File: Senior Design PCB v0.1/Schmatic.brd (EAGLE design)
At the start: 90.2 x 65.7 mm, 233 parts, among them IC1 TMC2208, IC2 TMC2208, IC3 TMC2208, IC4 TMC2208, IC5 TMC2208, IC6 CP2104, Q1 mmbt2222, Q2 mmbt2222, Q3 MMBT4403, Q4 AOD417, Q5 MMBT4403, Q6 MMBT4403, Q7 DMG3415U, U1 PCA9685, U2 AP2112-3.3, U3 HTU21DF, U4 HX711, U5 HX711, U6 HX711, X2 ESP32_WROOM32_SKINNY

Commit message: done all routing
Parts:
- removed C15, C22, C29: 0.1uF, SparkFun-Capacitors:0603-CAP
- removed C3: 560uF, SparkFun-Capacitors:PANASONIC_G
- removed D3: RED, microbuilder:CHIPLED_0805_NOOUTLINE
- removed R10: 1K, microbuilder:0603-NO@1
- moved U$4 19.2 mm to (-2.51, 4.82)
- moved U$48 18.4 mm to (92.2, 4.97)
- moved C68 13.5 mm to (6.86, 32.0), turned to 0 degrees
- moved R13 10.2 mm to (26.2, 48.0), turned to 270 degrees
- moved R34 8.92 mm to (55.1, 17.0)
- moved R52 8.03 mm to (26.7, 25.4), turned to 90 degrees
- moved R32 7.82 mm to (78.7, 23.6), turned to 0 degrees
- moved R31 6.68 mm to (79.8, 23.9), turned to 0 degrees
- moved SJ3 5.79 mm to (24.9, 42.2)
- moved C25 5.36 mm to (15.0, 54.9), turned to 270 degrees
- moved R1 4.77 mm to (61.7, 50.0), turned to 180 degrees
- moved R55 4.31 mm to (11.9, 10.9)
- moved R54 3.97 mm to (34.8, 22.9), turned to 270 degrees
- moved R28 3.75 mm to (78.0, 12.2), turned to 0 degrees
- moved C57 3.09 mm to (37.3, 17.3)
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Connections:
- net EN_3 renamed EN_LIQUID_1
- net EN_4 renamed EN_LIQUID_3
- net EN_5 renamed EN_LIQUID_2
- removed net DIR_3: IC3.19
- removed net DIR_4: IC4.19
- removed net DIR_5: IC5.19
- removed net EN_1: IC1.2, R33.2
- removed net EN_2: IC2.2, R40.2
- removed net MS1_1: IC1.9
- removed net MS1_2: IC2.9
- removed net MS1_3: IC3.9
- removed net MS1_4: IC4.9
- removed net MS1_5: IC5.9
- removed net MS2_1: IC1.10
- removed net MS2_2: IC2.10
- removed net MS2_3: IC3.10
- removed net MS2_4: IC4.10
- removed net MS2_5: IC5.10
- removed net N$5: D3.A, R10.2
- removed net STEP_3: IC3.16
- removed net STEP_4: IC4.16
- removed net STEP_5: IC5.16
- removed net VDD: C15.1, C22.1, C29.1
- new net DIR_LIQUID: IC3.19, IC4.19, IC5.19
- new net EN_XY: IC1.2, IC2.2, R33.2, R40.2
- new net MS1_LIQUID: IC3.9, IC4.9, IC5.9
- new net MS1_SOLID: IC1.9, IC2.9
- new net MS2_LIQUID: IC3.10, IC4.10, IC5.10
- new net MS2_SOLID: IC1.10, IC2.10
- new net STEP_LIQUID: IC3.16, IC4.16, IC5.16
- net 5V_SERVO: no longer C3.+
- net GND: no longer C15.2, C22.2, C29.2, C3.-, D3.C
- net ONBOARD_LED: no longer R10.1
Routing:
- net 5V_SERVO: track 4.20 -> 115.3 mm, vias 21 -> 53
- net SDA: track 5.41 -> 112.4 mm, vias 0 -> 4
- net SCL: track 5.88 -> 101.3 mm, vias 0 -> 3
- net VCC: track 9.40 -> 102.6 mm, vias 3 -> 36
- net 5V_REG: track 0.00 -> 89.7 mm, vias 18 -> 27
- net N$39: track 0.00 -> 65.3 mm
- net GND: track 321.4 -> 386.3 mm, vias 199 -> 193
- net N$40: track 0.00 -> 64.5 mm
- net N$38: track 0.00 -> 60.9 mm
- net MS2_LIQUID: track 0.00 -> 55.5 mm, vias 0 -> 4
- net N$50: track 0.00 -> 52.8 mm
- net RXD0: track 0.00 -> 52.0 mm, vias 0 -> 2
- net N$41: track 0.00 -> 51.9 mm, vias 0 -> 3
- net 12V_REG: track 23.6 -> 74.1 mm, vias 8 -> 19
- net MS1_LIQUID: track 0.00 -> 49.8 mm, vias 0 -> 3
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- added copper zone on layer 2, net 5V_SERVO
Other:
- board size 90.2 x 65.7 mm -> 101.3 x 66.8 mm

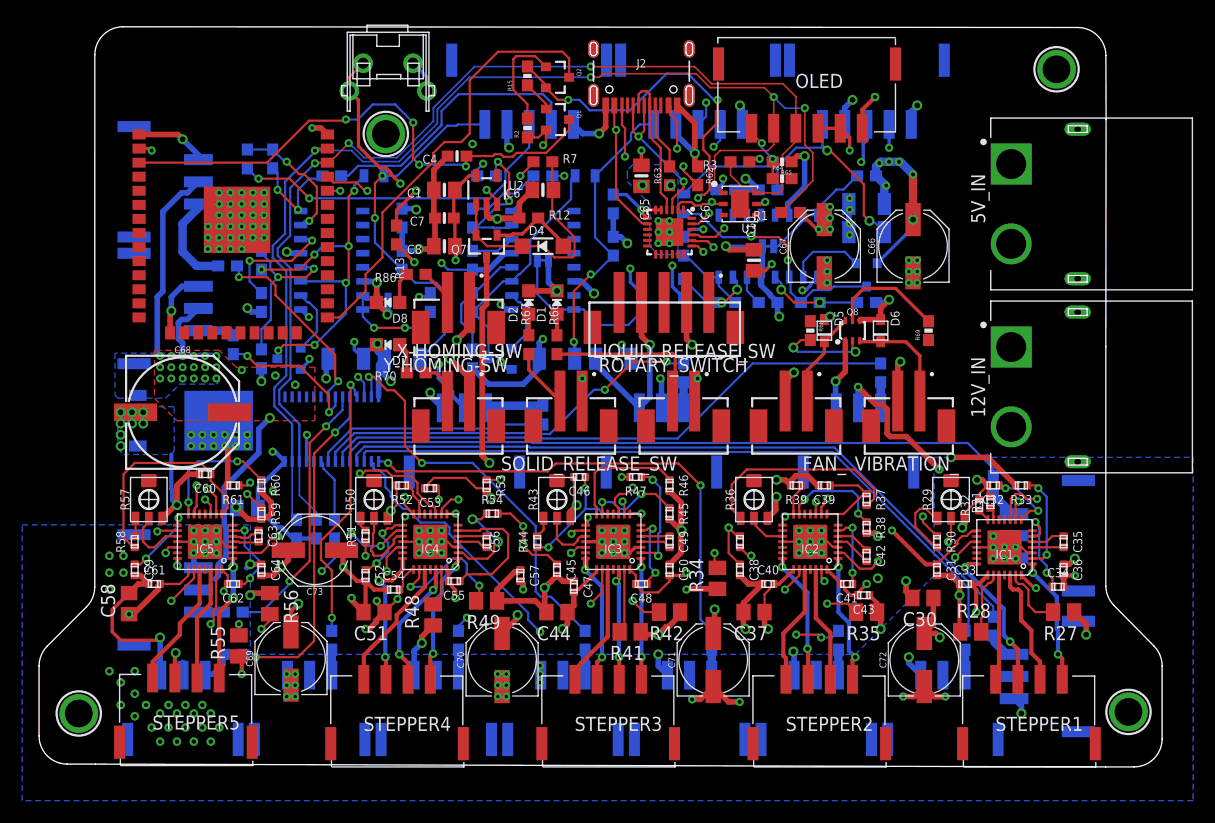
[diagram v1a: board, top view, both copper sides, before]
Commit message: update on i2c expander, fixed current pour
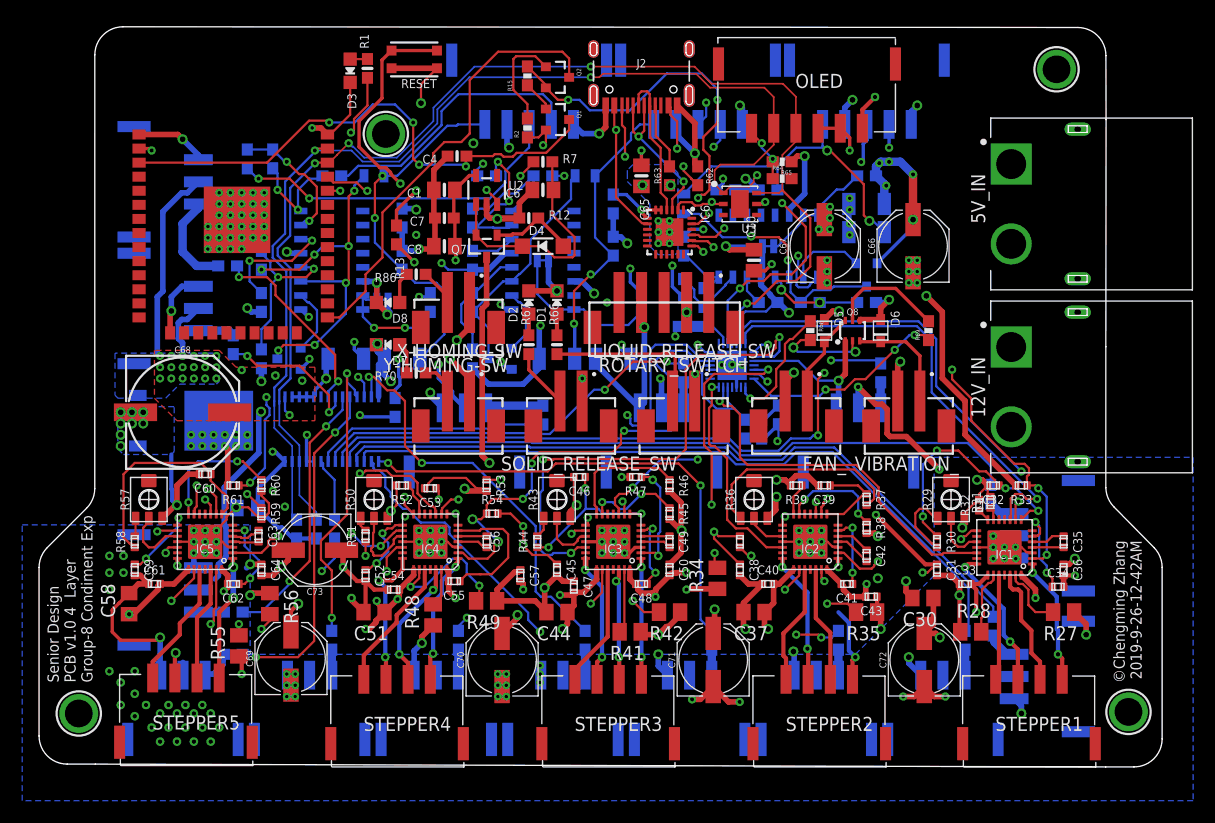
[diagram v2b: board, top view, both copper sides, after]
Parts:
- removed R3: 10k, SparkFun-Resistors:0603
- removed U$9: RIGHT_ANGLE_TACTILE_SWITCH, NewKevinMade:RIGHT_ANGLE_TACTILE_SWITCH
- added C15, C22, C3: 0.1uF, SparkFun-Capacitors:0603-CAP
- added D3: POWER, microbuilder:CHIPLED_0805_NOOUTLINE
- added R10: 10K, SparkFun-Resistors:0603-RES
- added R90: 10k, SparkFun-Resistors:0603
- added RESET: KMR2, microbuilder:BTN_KMR2_4.6X2.8
- added U7: SX1509, SparkFun-DigitalIC:QFN-28
- C11, C12, C13, C14, C18, C19, C20, C21, C25, C26, C27, C28: device SparkFun-Capacitors:0603-CAP -> SparkFun-Capacitors:0603-CAP@1
- R1: value 10k -> 1K; device SparkFun-Resistors:0603 -> microbuilder:0603-NO
- R11, R14, R17, R18, R19, R20, R22, R23, R24, R25, R5, R9: device SparkFun-Resistors:0603-RES -> SparkFun-Resistors:0603-RES@1
- R12, R66, R67, R7, R70, R86: device microbuilder:0603-NO@1 -> microbuilder:0603-NO
- SJ1, SJ2, SJ3: value (none) -> JUMPER-PAD-2-NC_BY_TRACE
- moved R1 40.3 mm to (23.5, 63.0), turned to 90 degrees
- moved C11 2.02 mm to (53.9, 42.4), turned to 90 degrees
- moved R71 0.83 mm to (79.8, 24.6)
- moved C43 0.69 mm to (69.0, 15.4)
- renumbered U$2 to WEIGHT3, U$5 to WEIGHT1, WEIGHT_SENSOR to WEIGHT2
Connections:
- removed net A0: U1.1
- removed net A1: U1.2
- removed net A2: U1.3
- removed net A3: U1.4
- removed net A4: U1.5
- removed net A5: U1.24
- new net !INT: U7.9
- new net !RESET: R10.1, U7.23
- new net 10: U7.15
- new net 11: U7.16
- new net 15: U7.22
- new net N$30: R90.1, U1.1
- new net N$5: D3.A, R1.2
- new net OSCIO: U7.11
- net DIR_1: now also U7.13
- net DIR_2: now also U7.14
- net DIR_LIQUID: now also U7.2
- net EN_LIQUID_1: now also U7.20
- net EN_LIQUID_2: now also U7.21
- net EN_LIQUID_3: now also U7.19
- net EN_XY: now also U7.1
- net FAN: now also U7.8
- net GND: now also C15.2, C22.2, C3.2, D3.C, RESET.A, RESET.A', U1.2, U1.24, U1.3, U1.4, U1.5, U7.10, U7.17, U7.26, U7.29, U7.3; no longer U$9.B_L, U$9.T_L
- net MS1_LIQUID: now also U7.5
- net MS1_SOLID: now also U7.27
- net MS2_LIQUID: now also U7.6
- net MS2_SOLID: now also U7.28
- net N$54: now also RESET.B, RESET.B'; no longer U$9.B_R, U$9.T_R
- net SCL: now also U7.25; no longer R3.2
- net SDA: now also U7.24; no longer R1.2
- net VCC: now also C15.1, C22.1, C3.1, R10.2, R90.2, U7.12, U7.18, U7.4; no longer R3.1
- net VIB: now also U7.7
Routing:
- net EN_LIQUID_2: track 12.0 -> 63.3 mm, vias 2 -> 4
- net DIR_LIQUID: track 45.0 -> 90.6 mm, vias 3 -> 5
- net GND: track 386.3 -> 427.5 mm, vias 193 -> 198
- net EN_XY: track 42.9 -> 83.3 mm, vias 4 -> 6
- net MS1_SOLID: track 22.3 -> 60.0 mm, vias 2 -> 3
- net MS2_SOLID: track 28.4 -> 63.7 mm
- net EN_LIQUID_3: track 9.44 -> 44.4 mm, vias 2 -> 5
- net DIR_1: track 0.00 -> 33.4 mm, vias 0 -> 1
- net MS1_LIQUID: track 49.8 -> 79.1 mm, vias 3 -> 6
- net VCC: track 102.6 -> 129.3 mm, vias 36 -> 37
- net EN_LIQUID_1: track 10.0 -> 32.2 mm, vias 2 -> 3
- net 5V_REG: track 89.7 -> 109.8 mm, vias 27 -> 29
- net DIR_2: track 0.00 -> 19.6 mm, vias 0 -> 1
- net VIB: track 0.00 -> 18.9 mm, vias 0 -> 3
- net MS2_LIQUID: track 55.5 -> 73.7 mm, vias 4 -> 6
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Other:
- outline, holes or cut-outs redrawn
- board text added: "Senior Design PCB v1.0 4 Layer Group-8 Condiment Exp"
- board text added: "©Chengming Zhang 2019-9-26-12-42AM"

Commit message: added contact board
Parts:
- removed SJ1, SJ2, SJ3: JUMPER-PAD-2-NC_BY_TRACE, SparkFun-Passives:PAD-JUMPER-2-NC_BY_TRACE_YES_SILK
- moved U$49 21.6 mm to (4.50, 63.1)
- moved R13 13.0 mm to (26.7, 61.0), turned to 0 degrees
- moved D3 12.1 mm to (9.85, 62.8), turned to 90 degrees
- moved R1 10.4 mm to (13.2, 62.9), turned to 180 degrees
- moved RESET 7.30 mm to (20.5, 63.2), turned to 0 degrees
- moved X2 6.48 mm to (5.08, 50.8), turned to 90 degrees
- moved R22 5.24 mm to (14.0, 49.8)
- moved R30 2.84 mm to (73.7, 22.9), turned to 0 degrees
- moved C25 1.80 mm to (13.7, 53.6)
- moved R40 1.72 mm to (57.2, 18.6)
- moved R82 1.44 mm to (11.1, 46.6)
- moved R71 1.27 mm to (79.8, 23.3)
- moved SERVO12 1.27 mm to (90.2, 25.4)
- moved C33 1.27 mm to (77.5, 15.2)
- moved C37 1.27 mm to (58.4, 12.7)
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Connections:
- removed net A13_I35: X2.7
- removed net A2_I34: X2.6
- removed net A5_IO4: X2.26
- removed net BUZZER: X2.10
- removed net CAP_OR_BAT: X2.14
- removed net CHARGE_OR_NOT: X2.16
- removed net IO15_A8: X2.23
- removed net IO21: X2.33
- removed net IO32_A7: X2.8
- removed net MISO: X2.31
- removed net MOSI: X2.30
- removed net N$10: R16.1, SJ2.2, U4.15, U4.16
- removed net N$18: R21.1, SJ1.2, U5.15, U5.16
- removed net N$25: R26.1, SJ3.2, U6.15, U6.16
- removed net ONBOARD_LED: X2.13
- removed net RX_CUS: X2.12
- removed net SCK: X2.29
- removed net SD_CS_MCU: X2.9
- removed net TX_CUS: X2.11
- net GND: now also R16.1, R21.1, R26.1, U4.15, U4.16, U5.15, U5.16, U6.15, U6.16; no longer SJ1.1, SJ2.1, SJ3.1
- net LRSW: now also X2.16
- net ROTA_A: now also X2.33
- net ROTA_C: now also X2.12
- net ROTA_E: now also X2.23
- net SRSW: now also X2.30
- net STEP_1: now also X2.26
- net STEP_2: now also X2.29
- net STEP_LIQUID: now also X2.31
- net WEIGHT_CLK_1: now also X2.9
- net WEIGHT_CLK_2: now also X2.11
- net WEIGHT_CLK_3: now also X2.14
- net WEIGHT_DATA_1: now also X2.8
- net WEIGHT_DATA_2: now also X2.10
- net WEIGHT_DATA_3: now also X2.13
- net X-HOMING: now also X2.6
- net Y-HOMING: now also X2.7
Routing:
- net STEP_1: track 0.00 -> 102.0 mm, vias 0 -> 9
- net STEP_2: track 0.00 -> 83.7 mm, vias 0 -> 5
- net WEIGHT_CLK_1: track 0.00 -> 77.2 mm, vias 0 -> 6
- net WEIGHT_DATA_1: track 0.00 -> 70.5 mm, vias 0 -> 4
- net SRSW: track 5.39 -> 65.7 mm, vias 0 -> 4
- net ROTA_A: track 0.00 -> 58.7 mm, vias 0 -> 3
- net STEP_LIQUID: track 49.3 -> 105.5 mm, vias 5 -> 8
- net ROTA_E: track 0.00 -> 55.3 mm, vias 0 -> 3
- net WEIGHT_DATA_2: track 0.00 -> 42.0 mm, vias 0 -> 4
- net ROTA_C: track 0.00 -> 41.6 mm, vias 0 -> 2
- net X-HOMING: track 3.90 -> 45.2 mm, vias 0 -> 2
- net WEIGHT_CLK_2: track 0.00 -> 36.5 mm, vias 0 -> 3
- net LRSW: track 14.9 -> 46.7 mm, vias 0 -> 2
- net SDA: track 123.8 -> 154.7 mm, vias 5 -> 7
- net Y-HOMING: track 4.37 -> 33.0 mm, vias 0 -> 3
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- added copper zone on layer 1, net 12V_REG
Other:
- board size 101.3 x 66.8 mm -> 101.3 x 67.6 mm

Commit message: v0.3
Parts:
- added OLED_RESET: KMR2, microbuilder:BTN_KMR2_4.6X2.8
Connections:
- removed net OLED_RST: R64.2
- new net N$18: OLED_RESET.A, OLED_RESET.A', R64.2
- net VCC: now also OLED_RESET.B, OLED_RESET.B'
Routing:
- net N$18: track 0.00 -> 23.9 mm
- net VCC: track 137.3 -> 146.5 mm, vias 36 -> 37
- net 12V_REG: track 75.9 -> 72.8 mm, vias 62 -> 61
- net STEP_LIQUID: track 105.5 -> 103.0 mm
- net SDA: track 154.7 -> 152.7 mm, vias 7 -> 8
- net 5V_SERVO: track 116.4 -> 117.6 mm
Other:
- board text added: "/Users/ChengMing/Desktop/SignatureLogo.bmp"

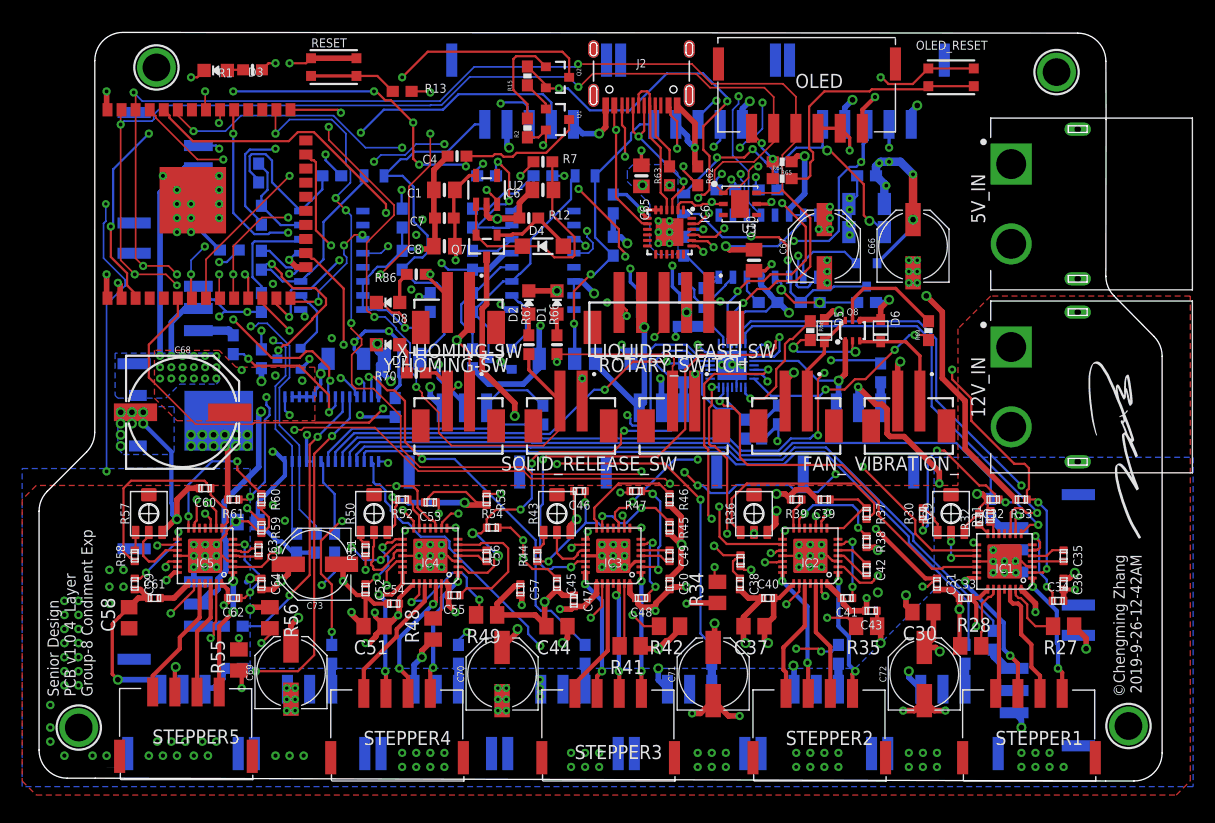
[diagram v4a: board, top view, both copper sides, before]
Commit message: added buck 12to5 3A
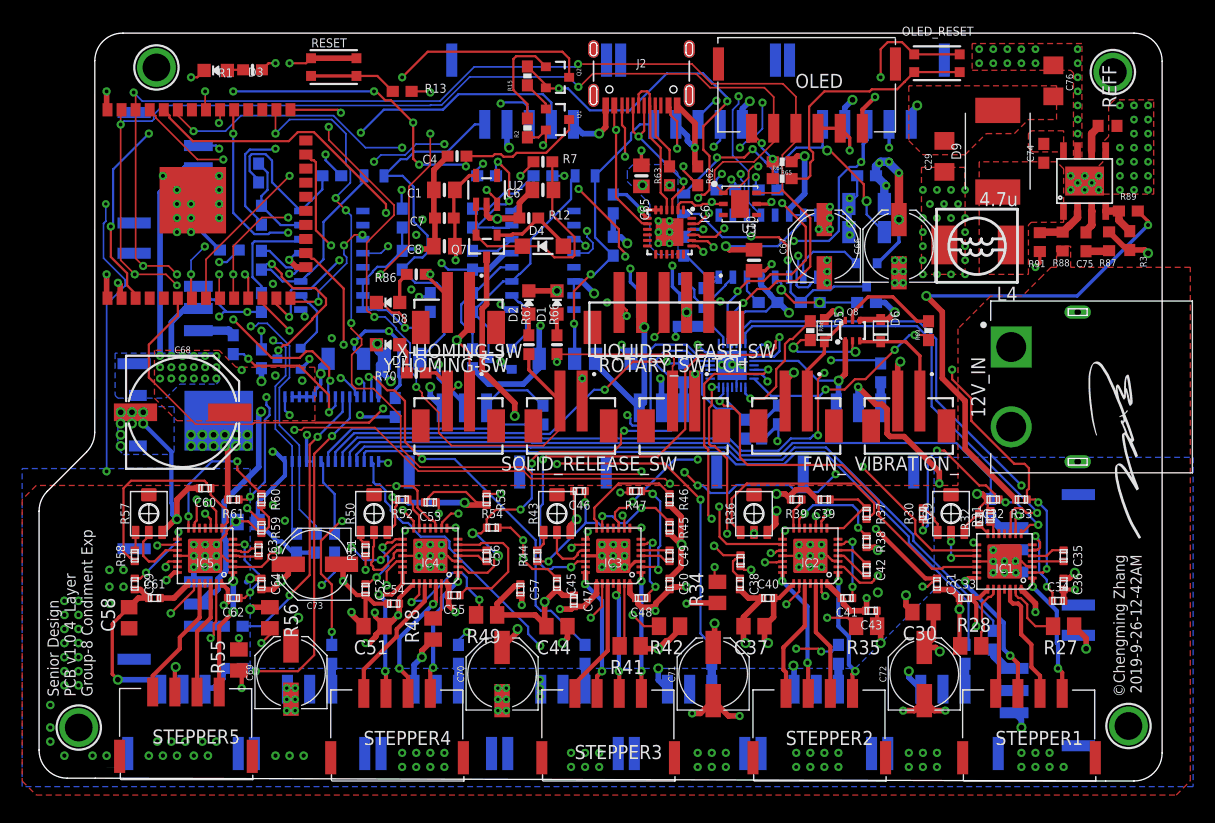
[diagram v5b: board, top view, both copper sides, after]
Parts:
- removed 5V_IN: XT60PW-M, XT60PW-M:AMASS_XT60PW-M
- added C29: 22u, adafruit:C1206
- added C74: 0.1u, adafruit:C0603
- added C75: 150p, adafruit:C0603
- added C76: 10u, adafruit:C1206
- added D9: SMD-DIODE-SCHOTTKY-40V-3A(DO-214AB), SMD-DIODE-SCHOTTKY-40V-3A_DO-214AB_:DO-214AB
- added L4: 4.7u, NewKevinMade:MHCI0603-4R7M-R8
- added R3: 210k, SparkFun-Resistors:0603
- added R87, R88, REFF: 100k, adafruit:R0603
- added R89: 40.2K, SparkFun-Resistors:0603
- added R91: 24k, adafruit:R0603
- added U$2: MP1584_V2, mp1584S:MP1584_V2
- moved U$50 5.08 mm to (90.8, 62.7)
- moved OLED_RESET 1.80 mm to (74.9, 63.5)
- moved C66 1.27 mm to (71.5, 47.0)
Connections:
- new net 5V_REG_EN: R88.1, R91.2, U$2.EN
- new net BST: C74.1, U$2.BST
- new net COMP: C75.1, U$2.COMP
- new net FB: R3.2, R89.1, U$2.FB
- new net FREQ: REFF.1, U$2.FREQ
- new net N$10: C75.2, R87.2
- new net SW: C74.2, D9.2, L4.P$1, U$2.SW
- net 12V_REG: now also C76.1, R88.2, U$2.VIN
- net 5V_REG: now also C29.1, L4.P$2, R89.2; no longer 5V_IN.1
- net GND: now also C29.2, C76.2, D9.1, R3.1, R87.1, R91.1, REFF.2, U$2.GND, U$2.GND_B; no longer 5V_IN.2
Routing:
- net 5V_REG: track 109.0 -> 133.3 mm, vias 29 -> 51
- net GND: track 454.7 -> 460.8 mm, vias 179 -> 208
- net 5V_REG_EN: track 0.00 -> 4.57 mm
- net 12V_REG: track 72.8 -> 68.7 mm, vias 61 -> 78
- net FB: track 0.00 -> 3.42 mm
- net FREQ: track 0.00 -> 2.52 mm
- net COMP: track 0.00 -> 2.16 mm
- net N$10: track 0.00 -> 2.10 mm
- net N$35: track 10.4 -> 9.08 mm
- net N$18: track 23.9 -> 23.2 mm
- added copper zone on layer 1, net 5V_REG
- added copper zone on layer 1, net BST
- added copper zone on layer 1, net GND
- added copper zone on layer 1, net SW
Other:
- board size 101.3 x 67.6 mm -> 101.3 x 67.5 mm
